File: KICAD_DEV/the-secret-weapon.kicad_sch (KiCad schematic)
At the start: 7 parts, among them J1 USB_C_Receptacle_USB2.0_14P, U1 STM32H757IITx, U2 TPS26750

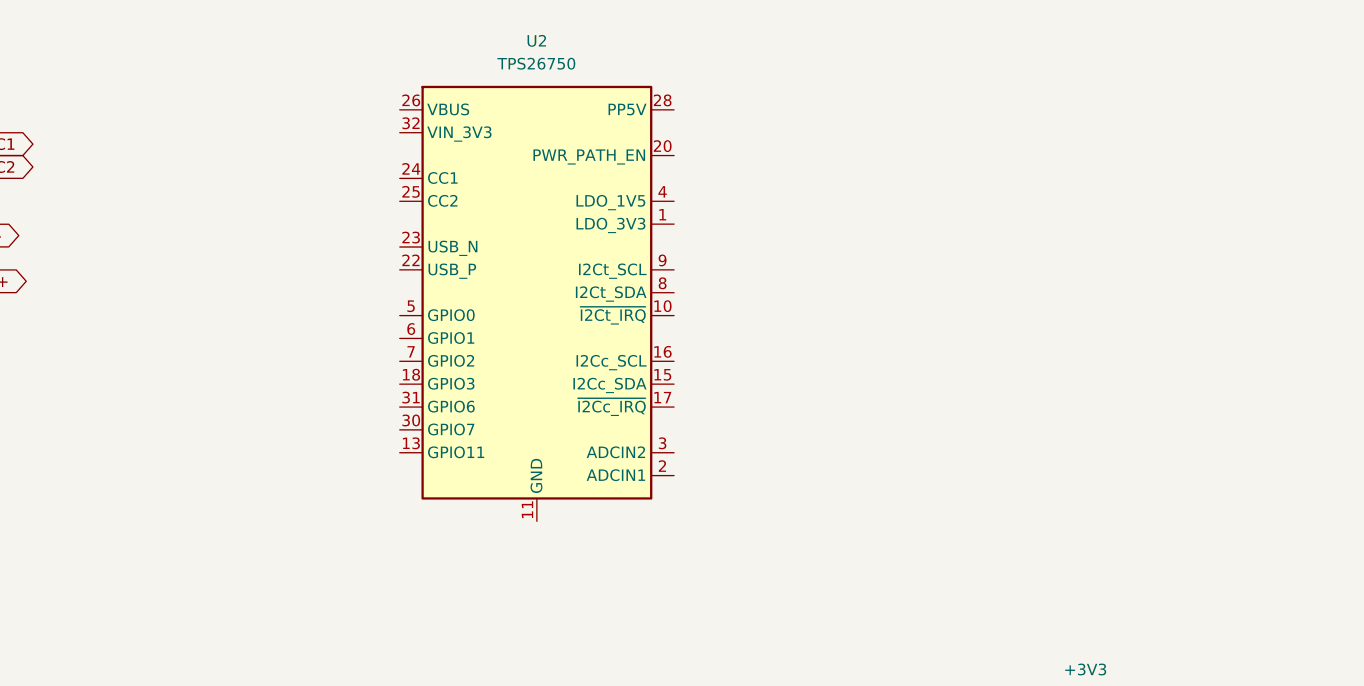
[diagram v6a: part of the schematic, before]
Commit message: starting to wire ESD
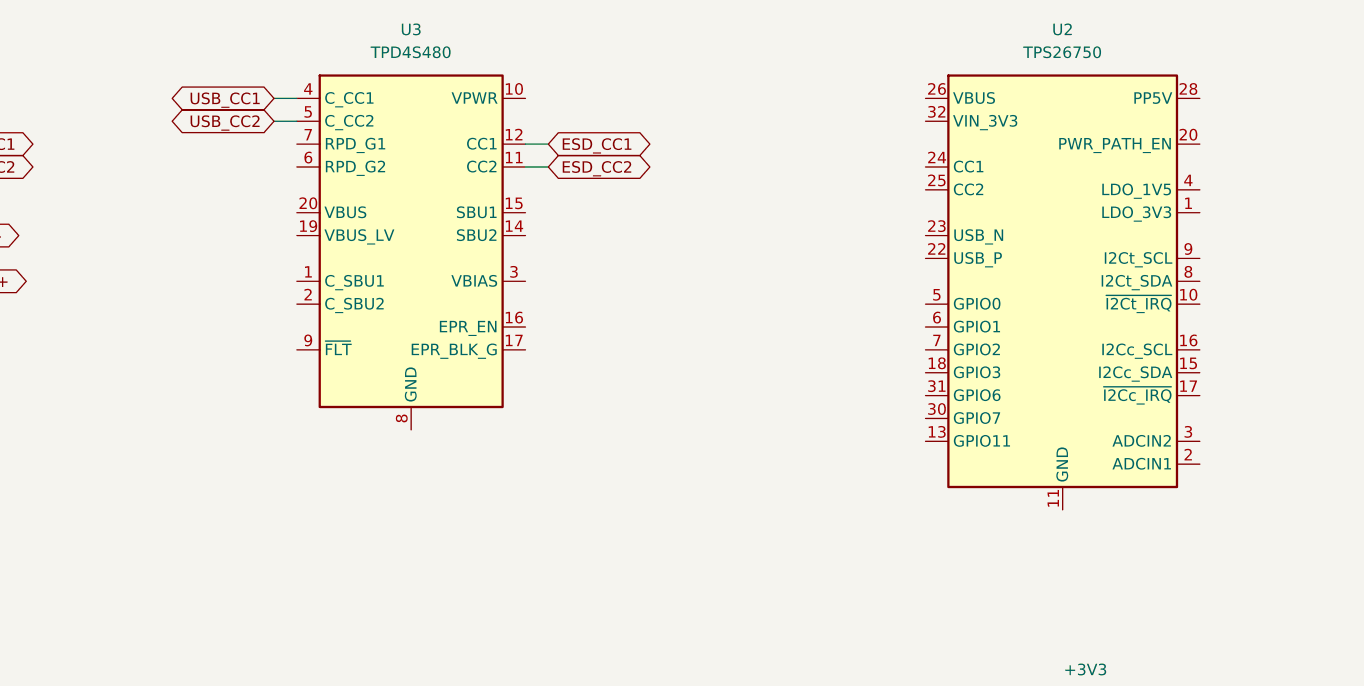
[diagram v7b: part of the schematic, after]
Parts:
- added U3: TPD4S480, Package_DFN_QFN:WQFN-20-1EP_3x3mm_P0.4mm_EP1.7x1.7mm_ThermalVias, symbol kai-library:TPD4S480
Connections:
- net USB_CC1: now also U3.4 (C_CC1)
- net USB_CC2: now also U3.5 (C_CC2)
- new net: U3.13 (GND), U3.16 (EPR_EN), U3.17 (EPR_BLK_G), U3.18 (GND), U3.21 (GND), U3.8 (GND)
- new net ESD_CC1: U3.12 (CC1)
- new net ESD_CC2: U3.11 (CC2)
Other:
- moved on the sheet: U2
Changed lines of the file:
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@@
+	(wire
+		(pts
+			(xy 148.59 50.8) (xy 151.13 50.8)
+		)
+		(stroke
+			(width 0)
+			(type default)
+		)
+	)
 	(wire
 		(pts
@@
 	(wire
 		(pts
+			(xy 179.07 55.88) (xy 176.53 55.88)
+		)
+		(stroke
+			(width 0)
+			(type default)
+		)
+	)
+	(wire
+		(pts
 			(xy 218.44 311.15) (xy 213.36 311.15)
 		)
@@
 	(wire
 		(pts
+			(xy 148.59 48.26) (xy 151.13 48.26)
+		)
+		(stroke
+			(width 0)
+			(type default)
+		)
+	)
+	(wire
+		(pts
 			(xy 266.7 119.38) (xy 269.24 119.38)
 		)
@@
 	(wire
 		(pts
+			(xy 179.07 53.34) (xy 176.53 53.34)
+		)
+		(stroke
+			(width 0)
+			(type default)
+		)
+	)
+	(wire
+		(pts
 			(xy 264.16 119.38) (xy 266.7 119.38)
 		)
@@
 			(width 0)
 			(type default)
+		)
+	)
+	(global_label "ESD_CC1"
+		(shape bidirectional)
+		(at 179.07 53.34 0)
+		(fields_autoplaced yes)
+		(effects
+			(font
+				(size 1.27 1.27)
+			)
+			(justify left)
+		)
+		(property "Intersheetrefs" "${INTERSHEET_REFS}"
+			(at 191.5121 53.34 0)
+			(effects
+				(font
+					(size 1.27 1.27)
+				)
+				(justify left)
+				(hide yes)
+			)
 		)
 	)
@@
 		)
 	)
+	(global_label "USB_CC2"
+		(shape bidirectional)
+		(at 148.59 50.8 180)
+		(fields_autoplaced yes)
+		(effects
+			(font
+				(size 1.27 1.27)
+			)
+			(justify right)
+		)
+		(property "Intersheetrefs" "${INTERSHEET_REFS}"
+			(at 135.9664 50.8 0)
+			(effects
+				(font
+					(size 1.27 1.27)
+				)
+				(justify right)
+				(hide yes)
+			)
+		)
+	)
 	(global_label "USB_D-"
 		(shape bidirectional)
@@
 				)
 				(justify left)
+				(hide yes)
+			)
+		)
+	)
+	(global_label "ESD_CC2"
+		(shape bidirectional)
+		(at 179.07 55.88 0)
+		(fields_autoplaced yes)
+		(effects
+			(font
+				(size 1.27 1.27)
+			)
+			(justify left)
+		)
+		(property "Intersheetrefs" "${INTERSHEET_REFS}"
+			(at 191.5121 55.88 0)
+			(effects
+				(font
+					(size 1.27 1.27)
+				)
+				(justify left)
+				(hide yes)
+			)
+		)
+	)
+	(global_label "USB_CC1"
+		(shape bidirectional)
+		(at 148.59 48.26 180)
+		(fields_autoplaced yes)
+		(effects
+			(font
+				(size 1.27 1.27)
+			)
+			(justify right)
+		)
+		(property "Intersheetrefs" "${INTERSHEET_REFS}"
+			(at 135.9664 48.26 0)
+			(effects
+				(font
+					(size 1.27 1.27)
+				)
+				(justify right)
 				(hide yes)
 			)
@@
 	(symbol
 		(lib_id "kai-library:TPS26750")
-		(at 177.8 64.77 0)
+		(at 236.22 63.5 0)
 		(unit 1)
 		(exclude_from_sim no)
@@
 		(fields_autoplaced yes)
 		(property "Reference" "U2"
-			(at 177.8 41.91 0)
+			(at 236.22 40.64 0)
 			(effects
 				(font
@@
 		)
 		(property "Value" "TPS26750"
-			(at 177.8 44.45 0)
+			(at 236.22 43.18 0)
 			(effects
 				(font
@@
 		)
 		(property "Footprint" "Package_DFN_QFN:Texas_RSN_WQFN-32-1EP_4x4mm_P0.4mm_EP2.8x2.8mm_ThermalVias"
-			(at 177.8 64.77 0)
+			(at 236.22 63.5 0)
 			(effects
 				(font
@@
 		)
 		(property "Datasheet" "https://www.ti.com/lit/ds/symlink/tps26750.pdf?ts=1761278028610&ref_url=https%253A%252F%252Fwww.ti.com%252Fproduct%252FTPS26750"
-			(at 177.8 64.77 0)
+			(at 236.22 63.5 0)
 			(effects
 				(font
@@
 		)
 		(property "Description" "TPS26750 USB Type-C® and USB PD Controller With Integrated Power Switches Optimized for Power Applications"
-			(at 177.8 64.77 0)
+			(at 236.22 63.5 0)
 			(effects
 				(font
@@
 					(unit 1)
 				)
+			)
+		)
+	)
+	(symbol
+		(lib_id "kai-library:TPD4S480")
+		(at 163.83 55.88 0)
+		(unit 1)
+		(exclude_from_sim no)
+		(in_bom yes)
+		(on_board yes)
+		(dnp no)
+		(fields_autoplaced yes)
+		(property "Reference" "U3"
+			(at 163.83 40.64 0)
+			(effects
+				(font
+					(size 1.27 1.27)
+				)
+			)
+		)
+		(property "Value" "TPD4S480"
+			(at 163.83 43.18 0)
+			(effects
+				(font
+					(size 1.27 1.27)
+				)
+			)
+		)
+		(property "Footprint" "Package_DFN_QFN:WQFN-20-1EP_3x3mm_P0.4mm_EP1.7x1.7mm_ThermalVias"
+			(at 163.83 55.88 0)
+			(effects
+				(font
+					(size 1.27 1.27)
+				)
+				(hide yes)
+			)
+		)
+		(property "Datasheet" "https://www.ti.com/lit/ds/symlink/tpd4s480.pdf?ts=1761346224525&ref_url=https%253A%252F%252Fwww.ti.com%252Fproduct%252FTPD4S480"
+			(at 163.83 55.88 0)
+			(effects
+				(font
+					(size 1.27 1.27)
+				)
+				(hide yes)
+			)
+		)
+		(property "Description" "TPD4S480 USB Type-C® 48V EPR Port Protector: Short-to-VBUS Overvoltage and IEC ESD Protection"
+			(at 163.83 55.88 0)
+			(effects
+				(font
+					(size 1.27 1.27)
+				)
+				(hide yes)
+			)
+		)
+		(pin "7"
+		)
+		(pin "17"
+		)
+		(pin "12"
+		)
+		(pin "15"
+		)
+		(pin "3"
+		)
+		(pin "2"
+		)
+		(pin "17"
+		)
+		(pin "14"
+		)
+		(pin "19"
+		)
+		(pin "4"
+		)
+		(pin "16"
+		)
+		(pin "20"
+		)
+		(pin "16"
+		)
+		(pin "10"
+		)
+		(pin "13"
+		)
+		(pin "1"
+		)
+		(pin "6"
+		)
+		(pin "11"
+		)
+		(pin "9"
+		)
+		(pin "21"
+		)
+		(pin "5"
+		)
+		(pin "8"
+		)
+		(pin "18"
+		)
+		(instances
+			(project ""
+				(path "/28389848-e686-45d1-8788-e912d76b51d3"
+					(reference "U3")
+					(unit 1)
+				)

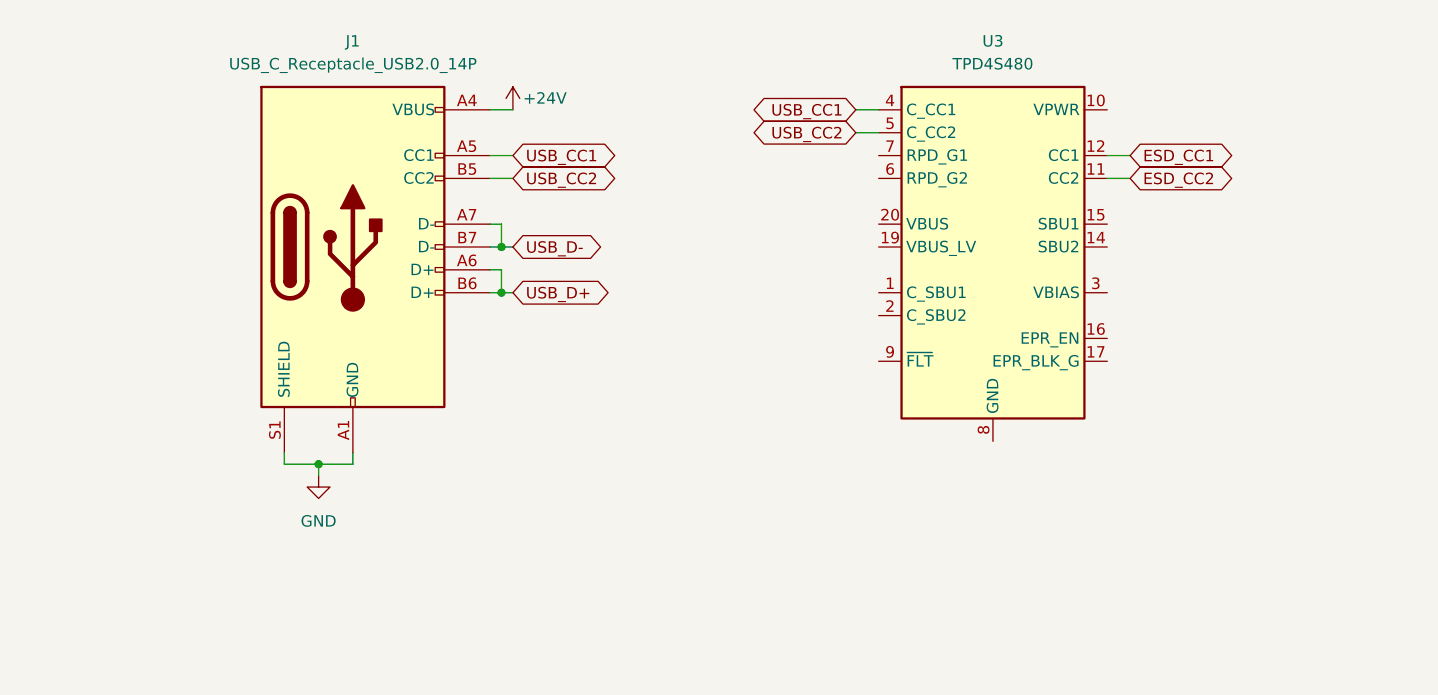
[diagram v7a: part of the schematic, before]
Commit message: more USB-C stuff
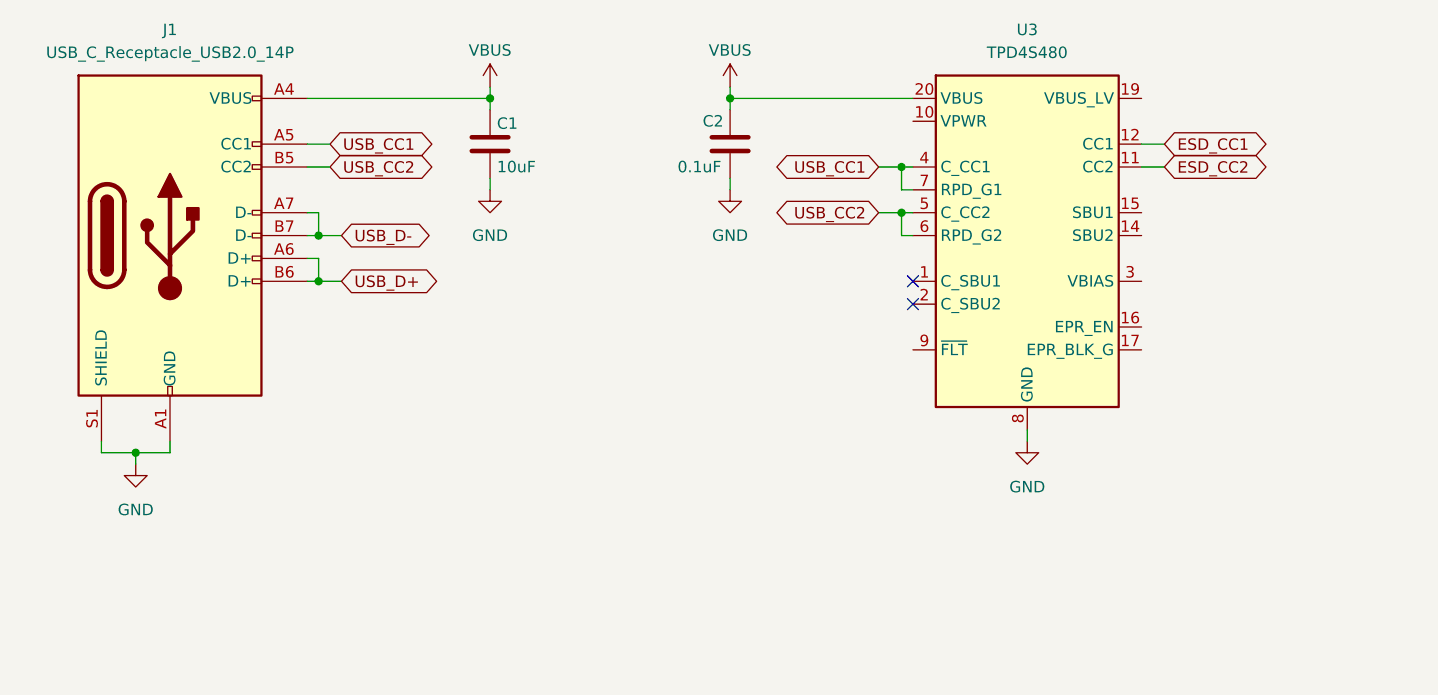
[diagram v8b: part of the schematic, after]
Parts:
- added C1: 10uF, symbol Device:C
- added C2: 0.1uF, symbol Device:C
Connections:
- net +24V is gone; now on net VBUS: J1.A4 (VBUS), J1.A9 (VBUS), J1.B4 (VBUS), J1.B9 (VBUS)
- net GND: now also U3.13 (GND), U3.16 (EPR_EN), U3.17 (EPR_BLK_G), U3.18 (GND), U3.21 (GND), U3.8 (GND), C1.2, C2.2
- net USB_CC1: now also U3.7 (RPD_G1)
- net USB_CC2: now also U3.6 (RPD_G2)
- net VBUS: now reaches U3.20 (VBUS)
- net VBUS: now also C1.1, C2.1
- no-connect marks 1 -> 3
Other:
- moved on the sheet: J1, U3
